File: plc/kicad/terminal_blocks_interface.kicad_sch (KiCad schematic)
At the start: 8 parts, among them CN1 DB128V-5.08-6P-GN-S, CN4 KF128-5.0-3P, CN5 KF128-5.0-3P, U1 LTV-814S-TA1-A, U4 TPS272C45ARHFR, U5 TPS272C45ARHFR

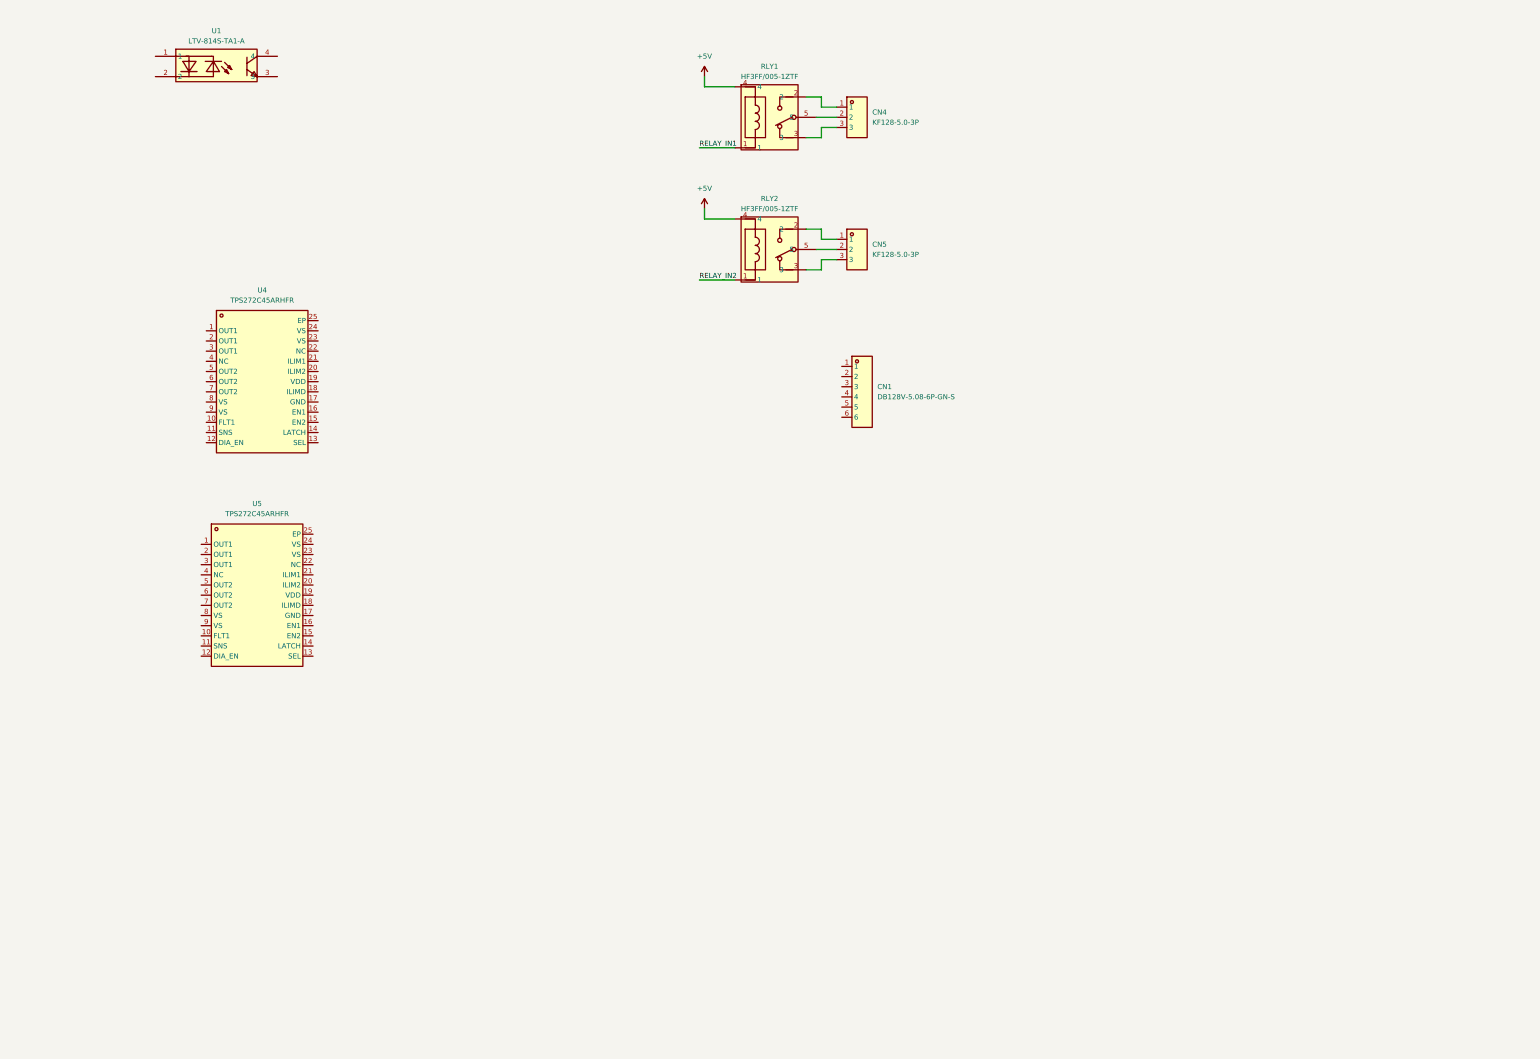
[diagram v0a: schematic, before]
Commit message: Added transistor outputs
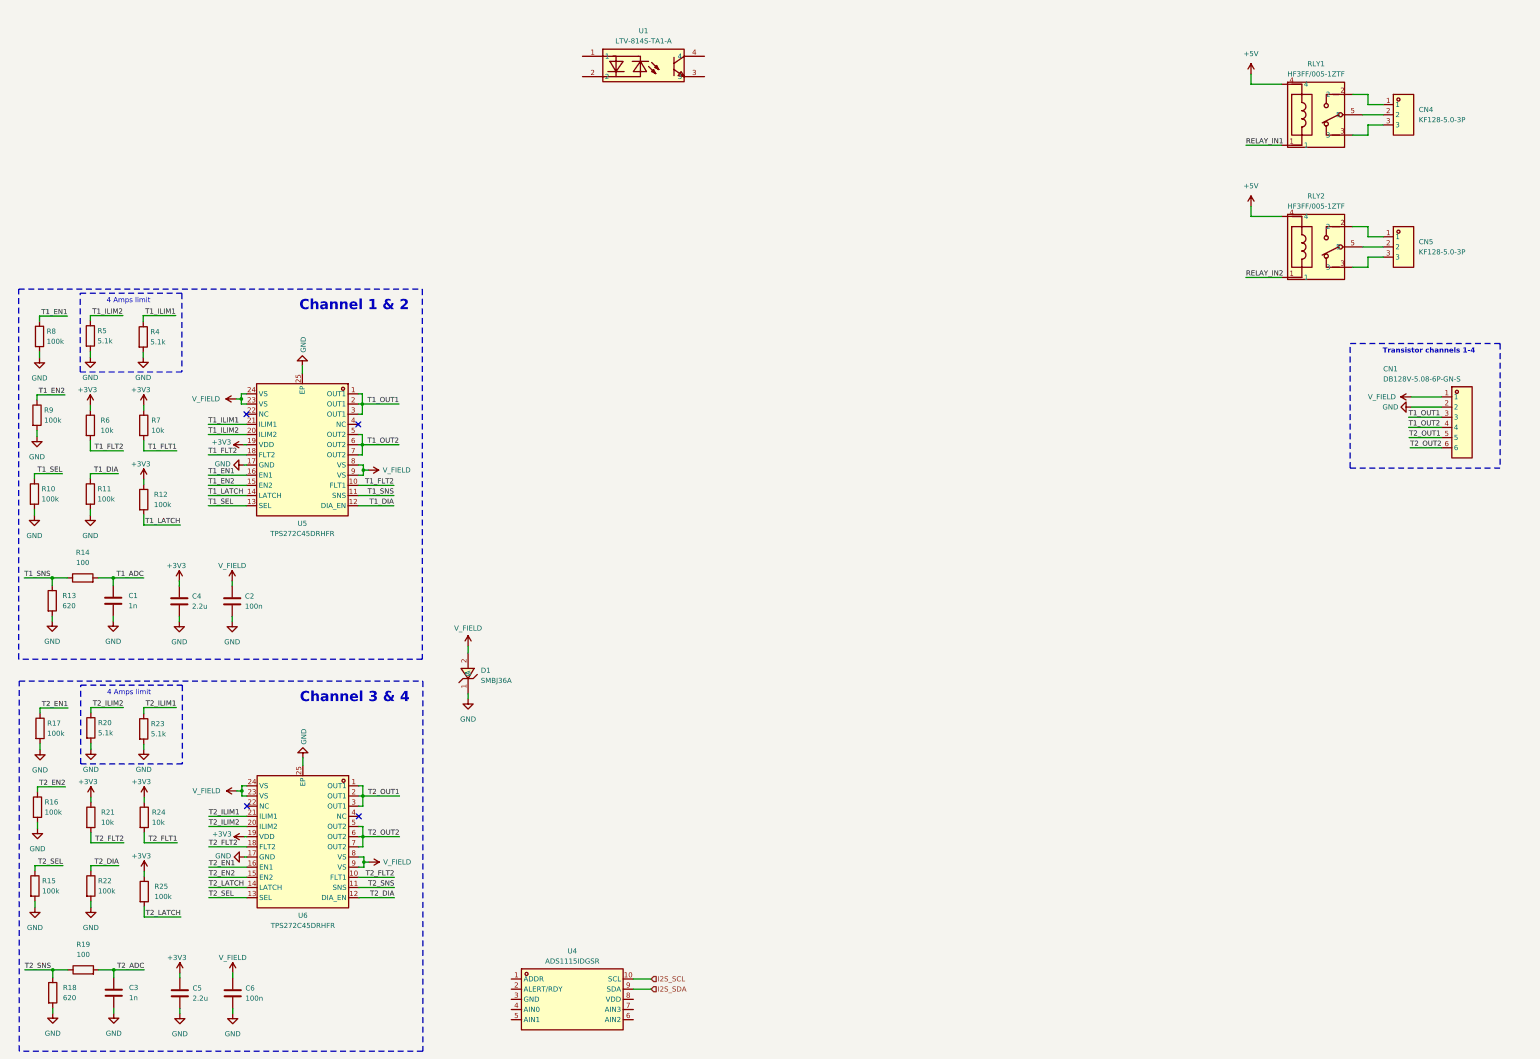
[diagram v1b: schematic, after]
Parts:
- removed U4, U5: TPS272C45ARHFR, LibrePLC32:VQFN-24_L5.0-W4.0-P0.50-BL-EP-1, symbol LibrePLC32:TPS272C45ARHFR
- added C1, C3: 1n, Capacitor_SMD:C_0805_2012Metric, symbol Device:C
- added C2, C6: 100n, Capacitor_SMD:C_0805_2012Metric, symbol Device:C
- added C4, C5: 2.2u, Capacitor_SMD:C_0805_2012Metric, symbol Device:C
- added D1: SMBJ36A, LibrePLC32:SMB_L4.6-W3.6-LS5.3-RD, symbol LibrePLC32:SMBJ36A-C114001
- added R10, R11, R12, R15, R16, R17, R22, R25, R8, R9: 100k, Resistor_SMD:R_0805_2012Metric, symbol Device:R
- added R13, R18: 620, Resistor_SMD:R_0805_2012Metric, symbol Device:R
- added R14, R19: 100, Resistor_SMD:R_0805_2012Metric, symbol Device:R
- added R20, R23, R4, R5: 5.1k, Resistor_SMD:R_0805_2012Metric, symbol Device:R
- added R21, R24, R6, R7: 10k, Resistor_SMD:R_0805_2012Metric, symbol Device:R
- added U4: ADS1115IDGSR, LibrePLC32:MSOP-10_L3.0-W3.0-P0.50-LS5.0-BL, symbol LibrePLC32:ADS1115IDGSR
- added U5, U6: TPS272C45DRHFR, LibrePLC32:VQFN-24_L5.0-W4.0-P0.50-BL-EP-1, symbol LibrePLC32:TPS272C45DRHFR
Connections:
- net V_FIELD: now reaches CN1.1
- net V_FIELD: now also C2.1, C6.1, D1.2 (A), U5.23 (VS), U5.24 (VS), U5.8 (VS), U5.9 (VS), U6.23 (VS), U6.24 (VS), U6.8 (VS), U6.9 (VS)
- net GND: now reaches CN1.2
- net GND: now also C1.2, C2.2, C3.2, C4.2, C5.2, C6.2, D1.1 (C), R10.2, R11.2, R13.2, R15.2, R16.2, R17.2, R18.2, R20.2, R22.2, R23.2, R4.2, R5.2, R8.2, R9.2, U5.17 (GND), U5.25 (EP), U6.17 (GND), U6.25 (EP)
- net T1_OUT1: now reaches CN1.3
- net T1_OUT1: now also U5.1 (OUT1), U5.2 (OUT1), U5.3 (OUT1)
- net T1_OUT2: now reaches CN1.4
- net T1_OUT2: now also U5.5 (OUT2), U5.6 (OUT2), U5.7 (OUT2)
- net T2_OUT1: now reaches CN1.5
- net T2_OUT1: now also U6.1 (OUT1), U6.2 (OUT1), U6.3 (OUT1)
- net T2_OUT2: now reaches CN1.6
- net T2_OUT2: now also U6.5 (OUT2), U6.6 (OUT2), U6.7 (OUT2)
- new net +3V3: C4.1, C5.1, R12.1, R21.1, R24.1, R25.1, R6.1, R7.1, U5.19 (VDD), U6.19 (VDD)
- new net I2S_SCL: U4.10 (SCL)
- new net I2S_SDA: U4.9 (SDA)
- new net T1_ADC: C1.1, R14.2
- new net T1_DIA: R11.1, U5.12 (DIA_EN)
- new net T1_EN1: R8.1, U5.16 (EN1)
- new net T1_EN2: R9.1, U5.15 (EN2)
- new net T1_FLT1: R7.2
- new net T1_FLT2: R6.2, U5.10 (FLT1), U5.18 (FLT2)
- new net T1_ILIM1: R4.1, U5.21 (ILIM1)
- new net T1_ILIM2: R5.1, U5.20 (ILIM2)
- new net T1_LATCH: R12.2, U5.14 (LATCH)
- new net T1_SEL: R10.1, U5.13 (SEL)
- new net T1_SNS: R13.1, R14.1, U5.11 (SNS)
- new net T2_ADC: C3.1, R19.2
- new net T2_DIA: R22.1, U6.12 (DIA_EN)
- new net T2_EN1: R17.1, U6.16 (EN1)
- new net T2_EN2: R16.1, U6.15 (EN2)
- new net T2_FLT1: R24.2
- new net T2_FLT2: R21.2, U6.10 (FLT1), U6.18 (FLT2)
- new net T2_ILIM1: R23.1, U6.21 (ILIM1)
- new net T2_ILIM2: R20.1, U6.20 (ILIM2)
- new net T2_LATCH: R25.2, U6.14 (LATCH)
- new net T2_SEL: R15.1, U6.13 (SEL)
- new net T2_SNS: R18.1, R19.1, U6.11 (SNS)
- no-connect marks 0 -> 4
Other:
- note added: "4 Amps limit"
- note added: "Channel 1 & 2"
- note added: "Channel 3 & 4"
- note added: "Transistor channels 1-4"
- moved on the sheet: CN1, CN4, CN5, RLY1, RLY2, U1

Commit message: Added gpio multiplexer and relay circuit
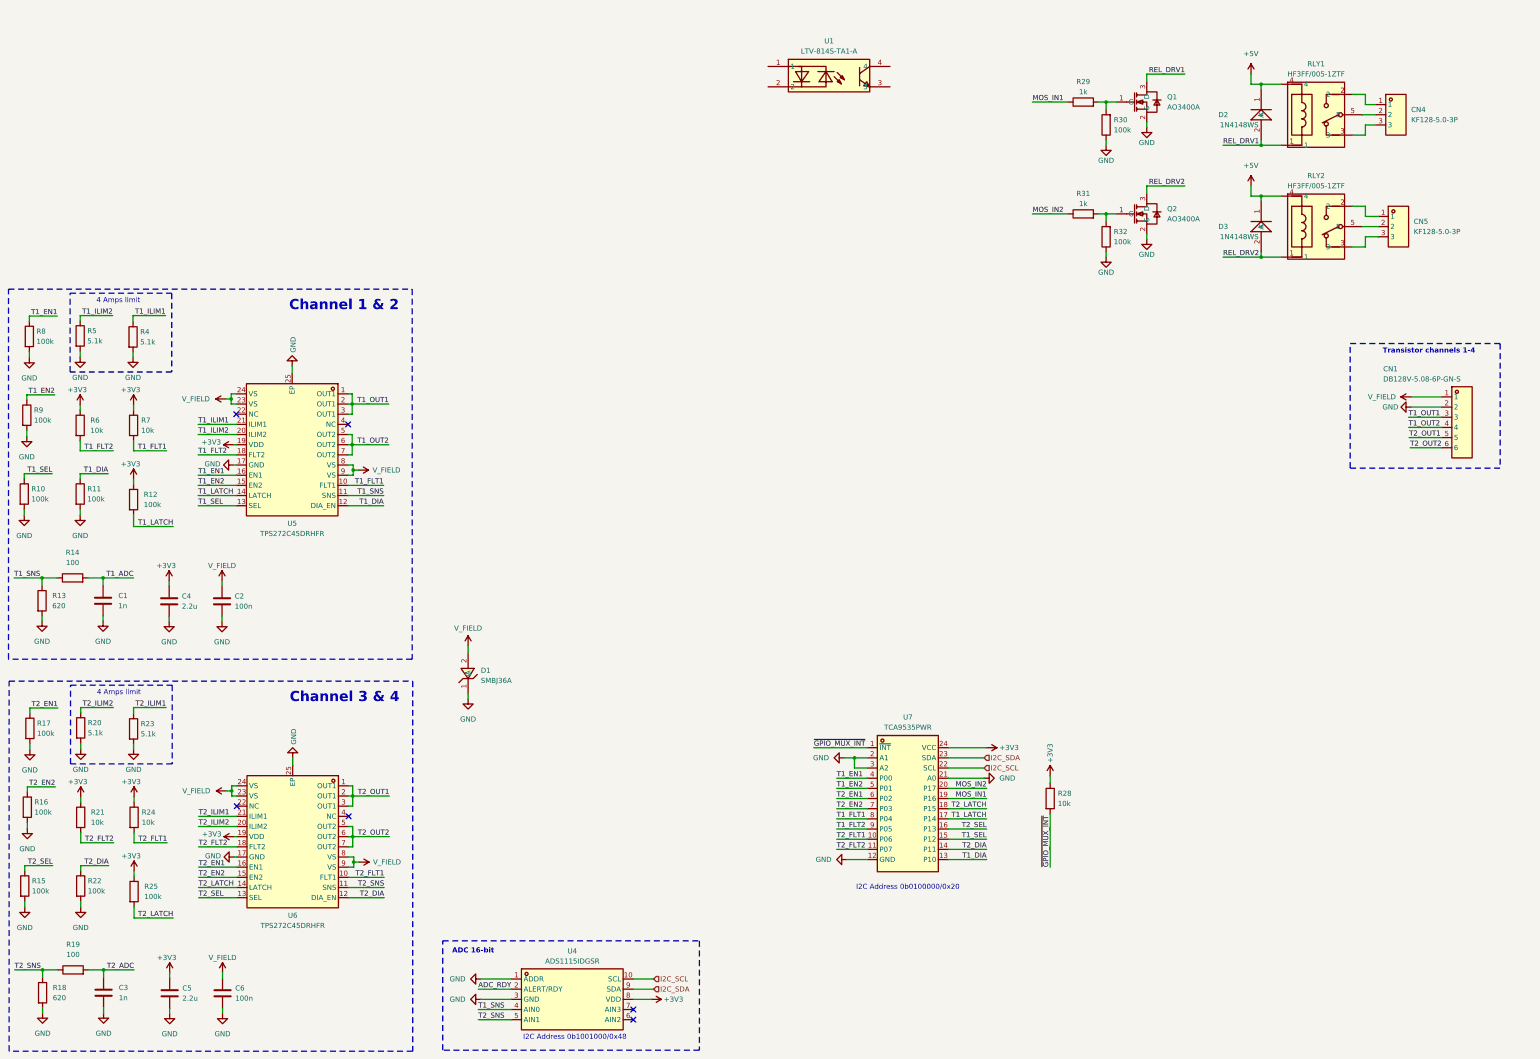
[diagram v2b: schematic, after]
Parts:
- added D2, D3: 1N4148WS, LibrePLC32:SOD-323_L1.8-W1.3-LS2.7-RD, symbol LibrePLC32:1N4148WS-E3-08
- added Q1, Q2: AO3400A, LibrePLC32:SOT-23-3_L2.9-W1.3-P1.90-LS2.4-BR, symbol LibrePLC32:AO3400A_C42419946
- added R28: 10k, Resistor_SMD:R_0805_2012Metric, symbol Device:R
- added R29, R31: 1k, Resistor_SMD:R_0805_2012Metric, symbol Device:R
- added R30, R32: 100k, Resistor_SMD:R_0805_2012Metric, symbol Device:R
- added U7: TCA9535PWR, LibrePLC32:TSSOP-24_L7.8-W4.4-P0.65-LS6.4-BL, symbol LibrePLC32:TCA9535PWR
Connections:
- net +3V3: now also U4.8 (VDD), R28.1, U7.24 (VCC)
- net +5V: now also D2.1 (K), D3.1 (K)
- net GND: now also U4.1 (ADDR), U4.3 (GND), Q1.2 (S), Q2.2 (S), R30.1, R32.1, U7.12 (GND), U7.2 (A1), U7.21 (A0), U7.3 (A2)
- net T1_DIA: now also U7.13 (P10)
- net T1_EN1: now also U7.4 (P00)
- net T1_EN2: now also U7.5 (P01)
- net T1_FLT1: now also U5.10 (FLT1), U7.8 (P04)
- net T1_FLT2: now also U7.9 (P05); no longer U5.10 (FLT1)
- net T1_LATCH: now also U7.17 (P14)
- net T1_SEL: now also U7.15 (P12)
- net T1_SNS: now also U4.4 (AIN0)
- net T2_DIA: now also U7.14 (P11)
- net T2_EN1: now also U7.6 (P02)
- net T2_EN2: now also U7.7 (P03)
- net T2_FLT1: now also U6.10 (FLT1), U7.10 (P06)
- net T2_FLT2: now also U7.11 (P07); no longer U6.10 (FLT1)
- net T2_LATCH: now also U7.18 (P15)
- net T2_SEL: now also U7.16 (P13)
- net T2_SNS: now also U4.5 (AIN1)
- net ADC_RDY: now reaches U4.2 (ALERT/RDY)
- net I2S_SCL renamed I2C_SCL
- net I2C_SCL: now also U7.22 (SCL)
- net I2S_SDA renamed I2C_SDA
- net I2C_SDA: now also U7.23 (SDA)
- net RELAY_IN1 renamed REL_DRV1
- net REL_DRV1: now also D2.2 (A), Q1.3 (D)
- net RELAY_IN2 renamed REL_DRV2
- net REL_DRV2: now also D3.2 (A), Q2.3 (D)
- new net: Q2.1 (G), R31.2, R32.2
- new net: Q1.1 (G), R29.2, R30.2
- new net MOS_IN1: R29.1, U7.19 (P16)
- new net MOS_IN2: R31.1, U7.20 (P17)
- new net ~{GPIO_MUX_INT}: R28.2, U7.1 (~{INT})
- no-connect marks 4 -> 6
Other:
- note added: "ADC 16-bit"
- note added: "I2C Address 0b0100000/0x20"
- note added: "I2C Address 0b1001000/0x48"
- moved on the sheet: C1, C2, C3, C4, C5, C6, CN4, R10, R11, R12, R13, R14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

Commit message: Updated ethernet circuit
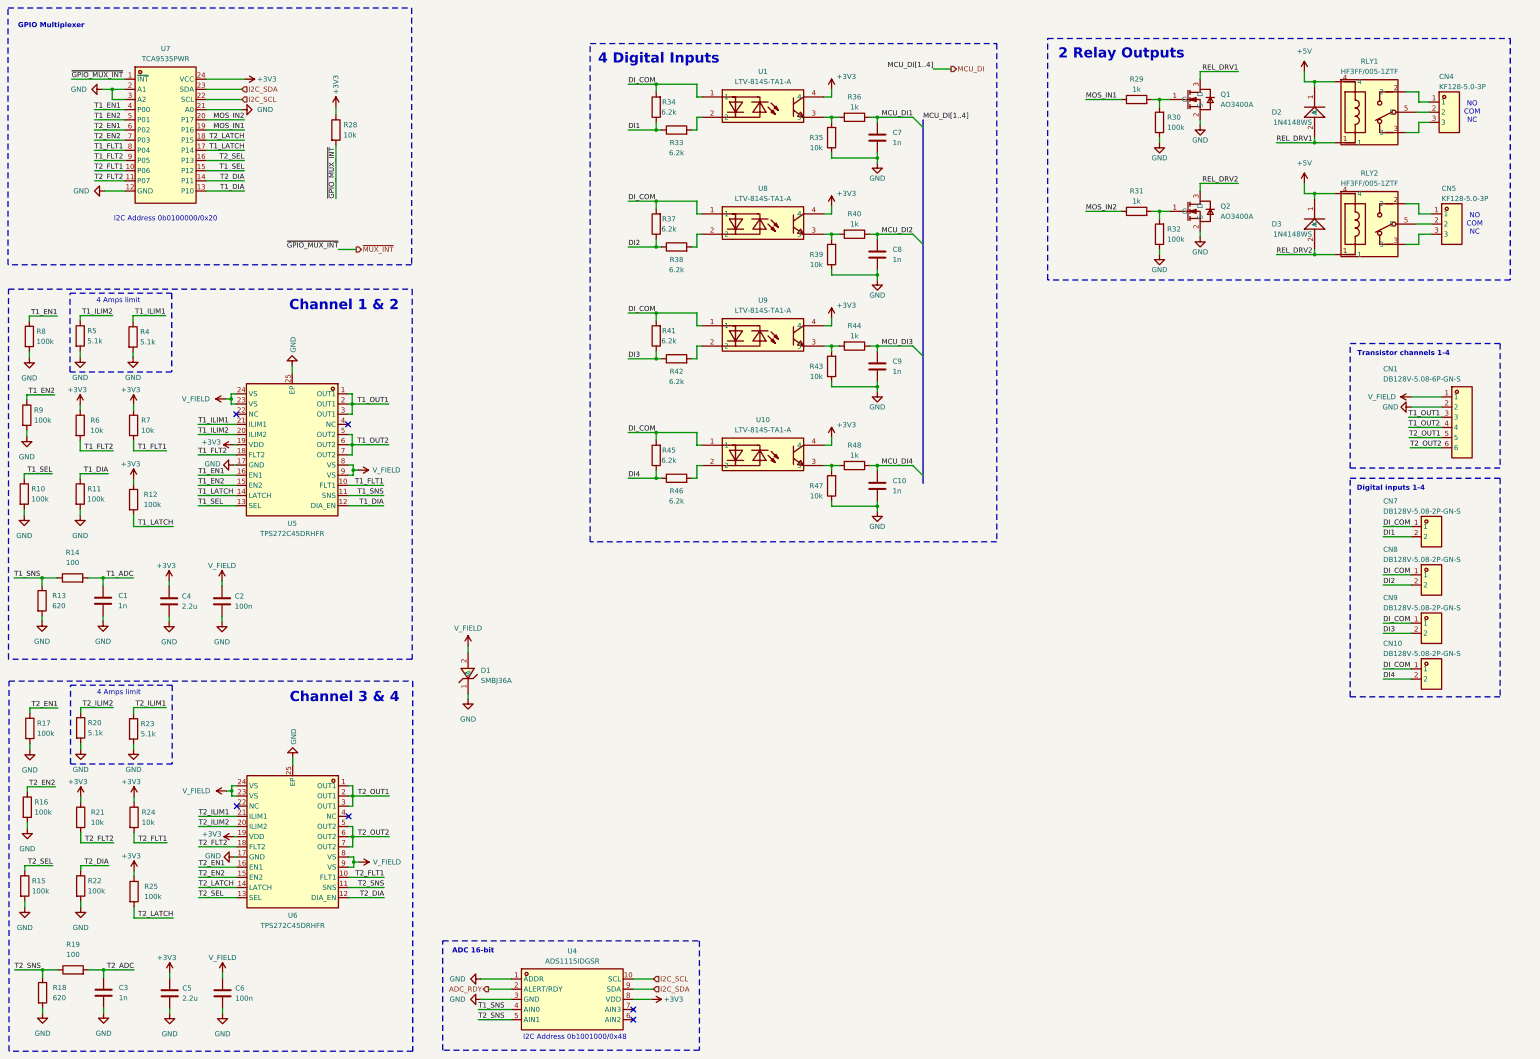
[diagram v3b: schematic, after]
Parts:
- added C10, C7, C8, C9: 1n, Capacitor_SMD:C_0805_2012Metric, symbol Device:C
- added CN10, CN7, CN8, CN9: DB128V-5.08-2P-GN-S, LibrePLC32:CONN-TH_2P-P5.08_DIBO_DB128V-5.08, symbol LibrePLC32:DB128V-5.08-2P-GN-S
- added R33, R34, R37, R38, R41, R42, R45, R46: 6.2k, Resistor_SMD:R_0805_2012Metric, symbol Device:R
- added R35, R39, R43, R47: 10k, Resistor_SMD:R_0805_2012Metric, symbol Device:R
- added R36, R40, R44, R48: 1k, Resistor_SMD:R_0805_2012Metric, symbol Device:R
- added U10, U8, U9: LTV-814S-TA1-A, LibrePLC32:OPTO-SMD-4_L4.6-W6.5-P2.54-LS10.3-BL, symbol LibrePLC32:LTV-814S-TA1-A
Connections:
- net +3V3: now also U1.4, U10.4, U8.4, U9.4
- net GND: now also C10.2, C7.2, C8.2, C9.2, R35.1, R39.1, R43.1, R47.1
- net DI_COM: now reaches U1.1
- net DI_COM: now also CN10.1, CN7.1, CN8.1, CN9.1, R34.2, R37.2, R41.2, R45.2, U10.1, U8.1, U9.1
- net at U1.2: now also R33.2
- net at U1.3: now also R35.2, R36.2
- net ~{GPIO_MUX_INT} renamed ~{MUX_INT}
- new net: R38.2, U8.2
- new net: R39.2, R40.2, U8.3
- new net: R43.2, R44.2, U9.3
- new net: R47.2, R48.2, U10.3
- new net: R46.2, U10.2
- new net: R42.2, U9.2
- new net DI1: CN7.2, R33.1, R34.1
- new net DI2: CN8.2, R37.1, R38.1
- new net DI3: CN9.2, R41.1, R42.1
- new net DI4: CN10.2, R45.1, R46.1
- new net MCU_DI1: C7.1, R36.1
- new net MCU_DI2: C8.1, R40.1
- new net MCU_DI3: C9.1, R44.1
- new net MCU_DI4: C10.1, R48.1
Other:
- note added: "2 Relay Outputs"
- note added: "4 Digital Inputs"
- note added: "Digital inputs 1-4"
- note added: "GPIO Multiplexer"
- note added: "NO COM NC"
- moved on the sheet: CN4, CN5, D2, D3, Q1, Q2, R28, R29, R30, R31, R32, RLY1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
